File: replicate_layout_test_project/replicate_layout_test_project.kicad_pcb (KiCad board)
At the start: 2 copper layers, 69 parts, among them J1001 Pusa_6mm, J1002 Pusa_6mm, J201 Pusa_6mm, J202 Pusa_6mm, J601 Pusa_6mm, J602 Pusa_6mm, Q1101 CSD19531KCS, Q1102 CSD19531KCS, Q1301 CSD19531KCS, Q1302 CSD19531KCS, Q1401 CSD19531KCS, Q1402 CSD19531KCS, Q301 CSD19531KCS, Q302 CSD19531KCS, Q501 CSD19531KCS, Q502 CSD19531KCS, Q701 CSD19531KCS, Q702 CSD19531KCS, Q901 CSD19531KCS, Q902 CSD19531KCS, U101 TMS320F28027DA, U1101 IR2181, U1201 INA240A1D, U1301 IR2181, U1401 IR2181, U301 IR2181, U401 INA240A1D, U501 IR2181, U701 IR2181, U801 INA240A1D, U901 IR2181

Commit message: Towards flip replication
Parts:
- C702, Q701, Q702, R701, R702, U701: moved to B.Cu
- moved Q702 67.1 mm to (153.0, 65.9), turned to 135 degrees
- moved R702 63.6 mm to (148.9, 69.9), turned to 45 degrees
- moved C702 62.3 mm to (151.6, 78.0), turned to 135 degrees
- moved C701 60.9 mm to (145.3, 79.8), turned to -135 degrees
- moved U701 59.0 mm to (147.6, 81.1), turned to 45 degrees
- moved R701 57.2 mm to (157.0, 78.0), turned to 45 degrees
- moved D701 49.1 mm to (152.5, 82.5), turned to -135 degrees
- moved Q701 45.5 mm to (161.0, 74.0), turned to 125 degrees
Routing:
- net GND: track 103.8 -> 31.4 mm, vias 3 -> 1
- net /Full Bridge1/Leg+/VS: track 0.00 -> 30.9 mm
- net +15V: track 30.9 -> 10.3 mm, vias 3 -> 1
- net Net-(R702-Pad1): track 0.00 -> 13.7 mm
- net Net-(R701-Pad1): track 0.00 -> 7.89 mm
- net /Full Bridge1/Q_high: track 0.00 -> 7.46 mm
- net /Full Bridge1/Q_low: track 0.00 -> 6.82 mm
- net /Full Bridge1/Leg+/VB: track 0.00 -> 6.10 mm, vias 0 -> 1
- net Net-(Q702-Pad1): track 0.00 -> 4.22 mm
- net Net-(Q701-Pad1): track 0.00 -> 4.21 mm
- added copper zone on B.Cu, net /Full Bridge1/Leg+/VS

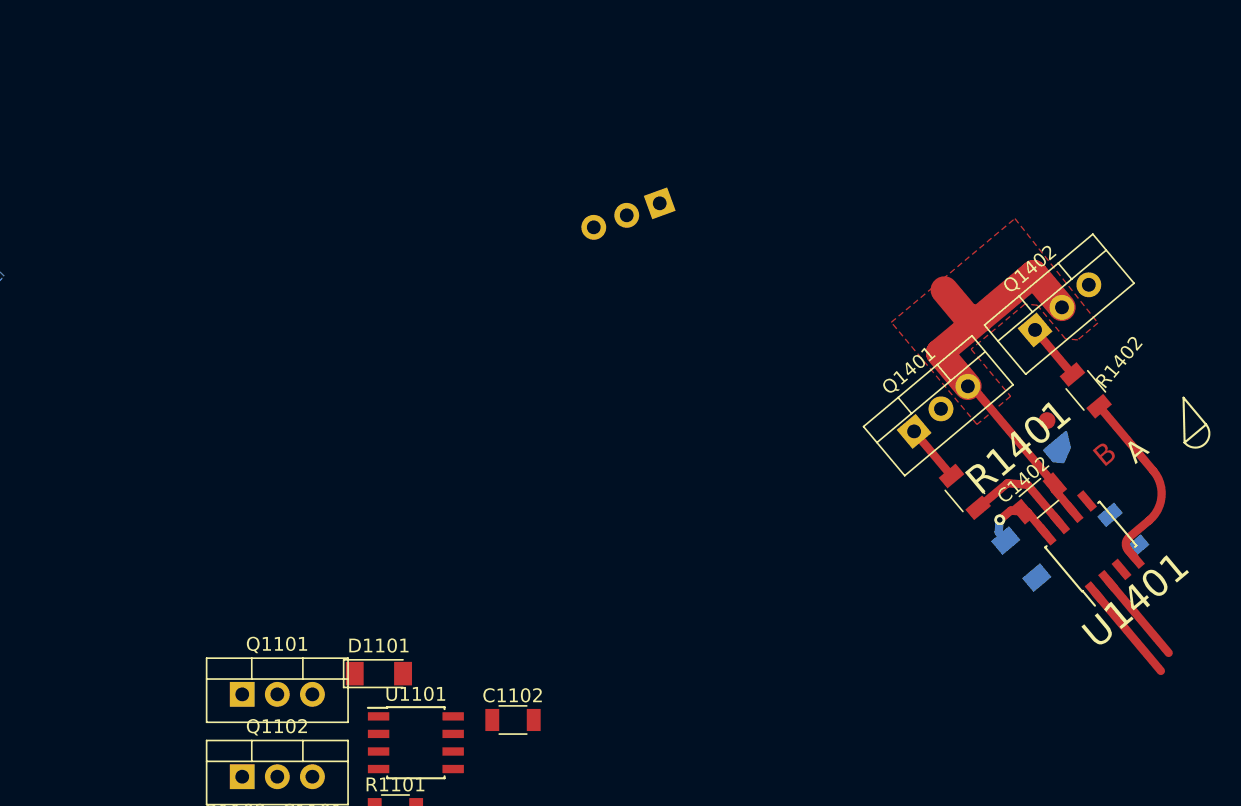
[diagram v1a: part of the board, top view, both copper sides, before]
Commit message: Solved fp_text replication
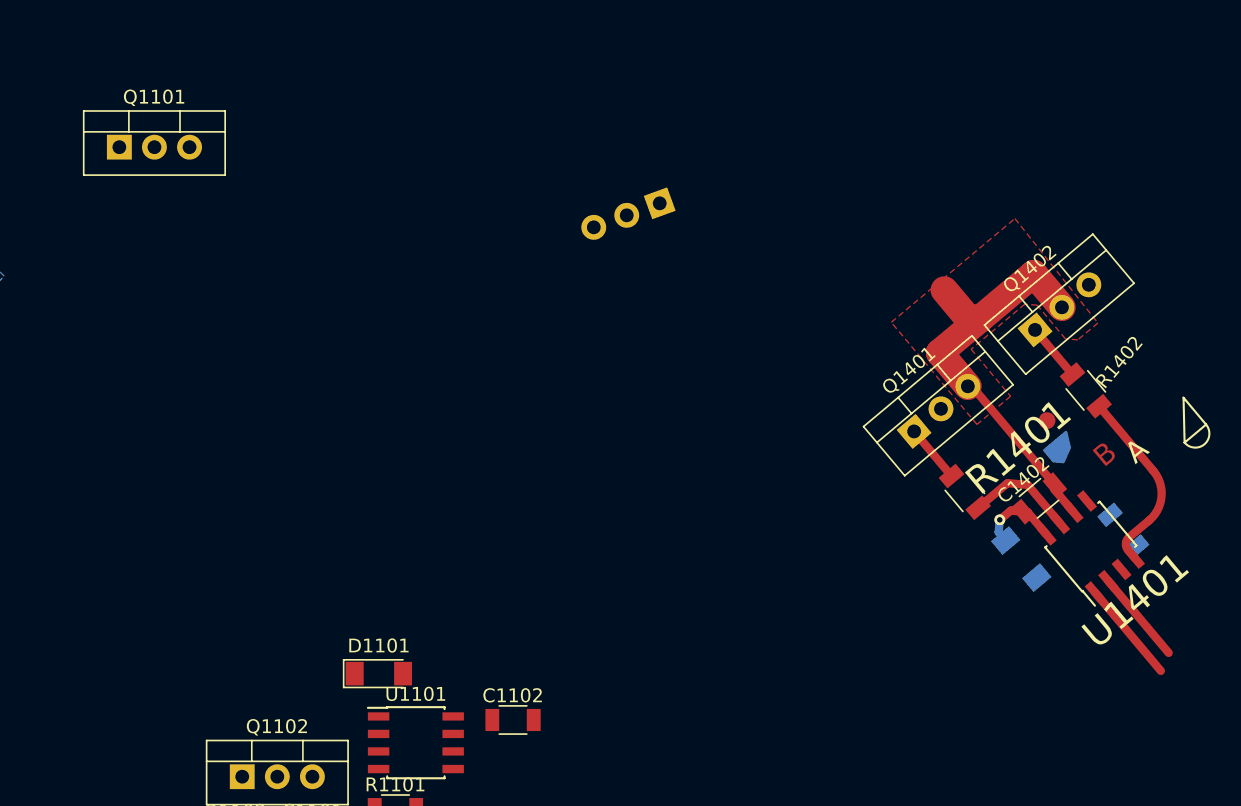
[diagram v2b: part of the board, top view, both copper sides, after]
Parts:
- moved Q1101 40.6 mm to (171.7, 56.9)
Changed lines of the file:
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@@
     (fp_line (start 1 -1.02) (end -1 -1.02) (layer "F.SilkS") (width 0.12))
     (fp_line (start -1 1.02) (end 1 1.02) (layer "F.SilkS") (width 0.12))
-    (fp_line (start 2.25 1.05) (end 2.25 -1.05) (layer "F.CrtYd") (width 0.05))
     (fp_line (start -2.25 -1.05) (end 2.25 -1.05) (layer "F.CrtYd") (width 0.05))
     (fp_line (start 2.25 1.05) (end -2.25 1.05) (layer "F.CrtYd") (width 0.05))
+    (fp_line (start 2.25 1.05) (end 2.25 -1.05) (layer "F.CrtYd") (width 0.05))
     (fp_line (start -2.25 -1.05) (end -2.25 1.05) (layer "F.CrtYd") (width 0.05))
     (fp_line (start 1.6 0.8) (end -1.6 0.8) (layer "F.Fab") (width 0.1))
@@
   )
   (footprint "Discretes:TO-220" (layer "F.Cu")
-    (at 180.6 96.505)
+    (at 171.704 56.896)
     (descr "TO-220-3, Vertical, RM 2.54mm")
     (tags "TO-220-3 Vertical RM 2.54mm")
@@
     ) (layer "B.Cu") (width 0.2) (fill solid))
   (gr_line (start 140.022201 71.620133) (end 141.818252 69.824082) (layer "B.SilkS") (width 0.15))
-  (gr_arc (start 141.459042 73.056974) (mid 140.022201 73.056975) (end 140.022201 71.620133) (layer "B.SilkS") (width 0.15))
+  (gr_arc (start 141.459042 73.056974) (mid 140.0222 73.056975) (end 140.022201 71.620133) (layer "B.SilkS") (width 0.15))
   (gr_line (start 141.818252 69.824082) (end 141.459042 73.056974) (layer "B.SilkS") (width 0.15))
   (gr_line (start 141.459042 73.056974) (end 140.022201 71.620133) (layer "B.SilkS") (width 0.15))
-  (gr_arc (start 250.372333 76.975492) (mid 250.247104 78.406865) (end 248.81573 78.281636) (layer "F.SilkS") (width 0.15))
+  (gr_arc (start 250.372333 76.975492) (mid 250.247103 78.406866) (end 248.81573 78.281636) (layer "F.SilkS") (width 0.15))
   (gr_line (start 250.372333 76.975492) (end 248.81573 78.281636) (layer "F.SilkS") (width 0.15))
   (gr_line (start 86.36 86.868) (end 86.36 89.408) (layer "F.SilkS") (width 0.15))
@@
   (arc (start 99.06 92.71) (mid 99.245987 92.260987) (end 99.695 92.075) (width 0.6) (layer "F.Cu") (net 40))
   (arc (start 101.6 92.075) (mid 103.396051 91.331051) (end 104.14 89.535) (width 0.6) (layer "F.Cu") (net 40))
+  (segment (start 153.975539 77.09809) (end 155.934225 79.056775) (width 0.6) (layer "B.Cu") (net 41))
   (segment (start 149.923817 79.679029) (end 152.504757 77.09809) (width 0.6) (layer "B.Cu") (net 41))
-  (segment (start 153.975539 77.09809) (end 155.934225 79.056775) (width 0.6) (layer "B.Cu") (net 41))
   (segment (start 152.504757 77.09809) (end 153.975539 77.09809) (width 0.6) (layer "B.Cu") (net 41))
   (segment (start 144.309389 81.701355) (end 144.871539 81.139205) (width 0.6) (layer "B.Cu") (net 42))

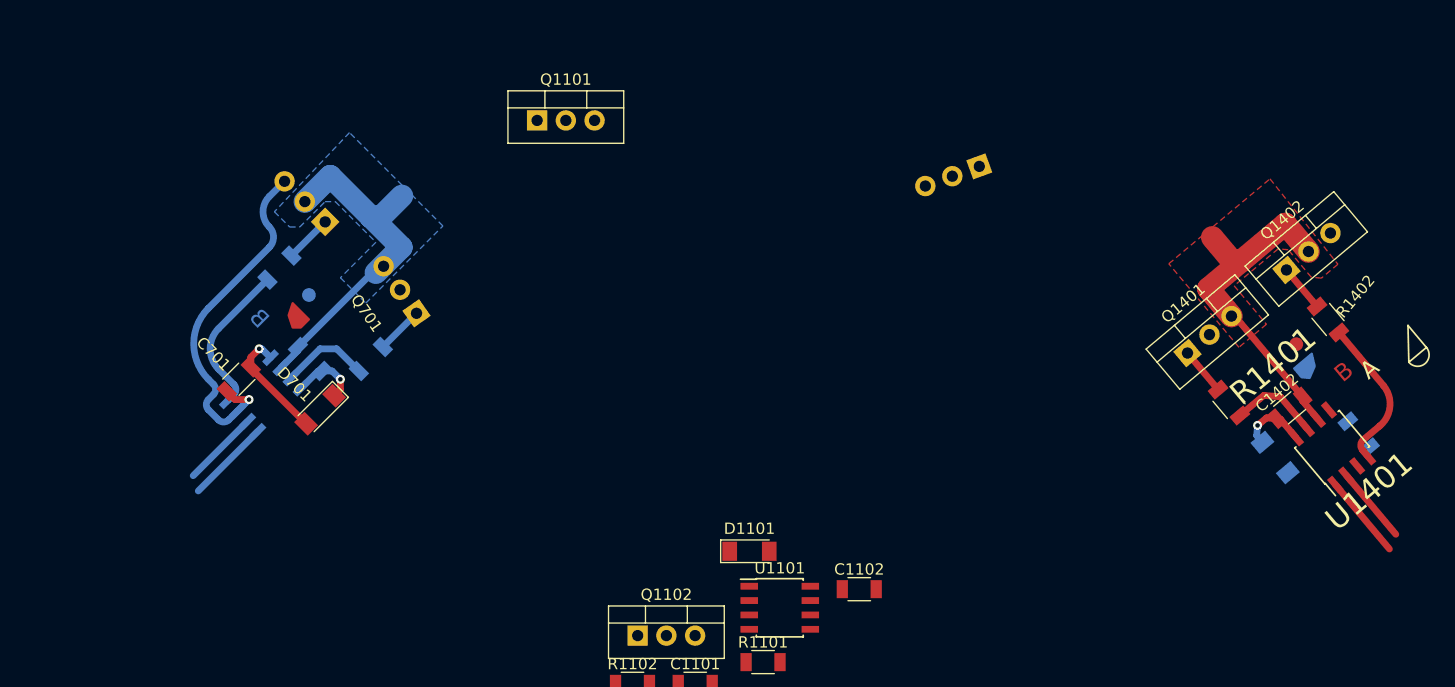
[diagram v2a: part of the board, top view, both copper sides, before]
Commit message: Added support for replicating grouped items only
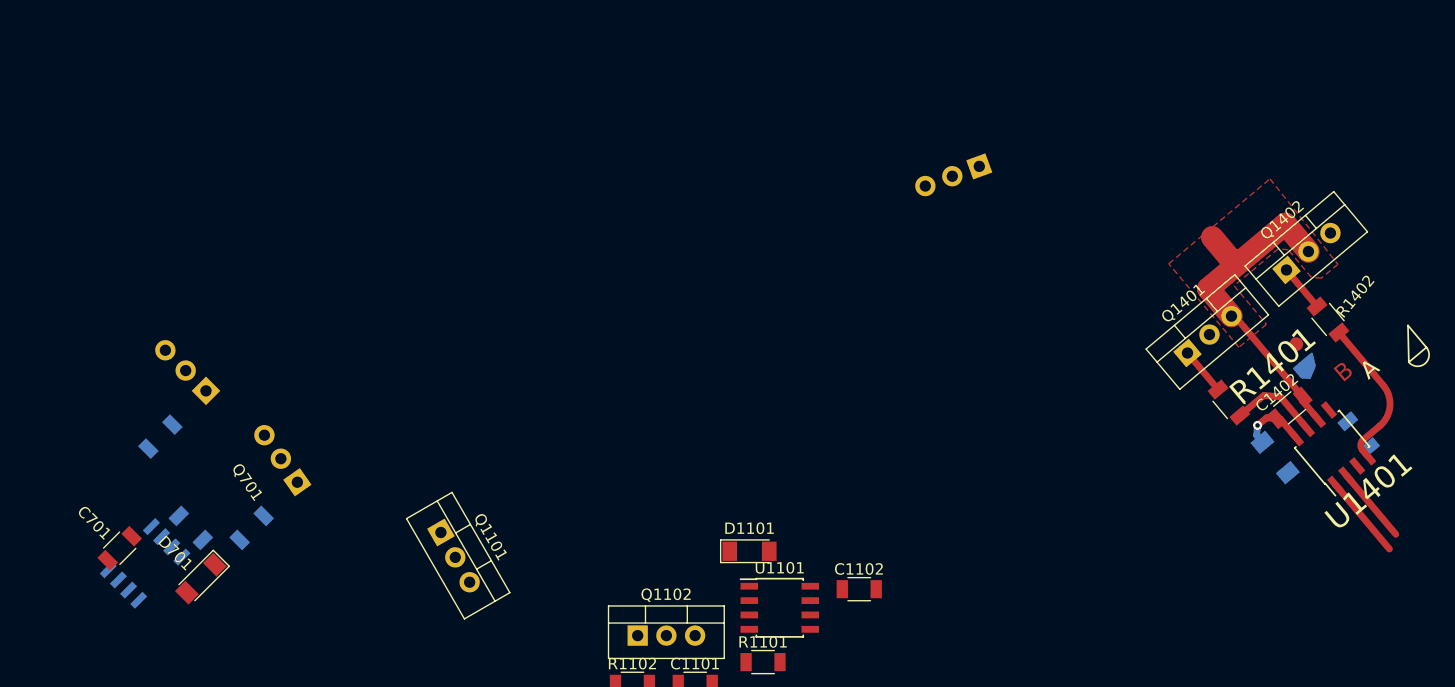
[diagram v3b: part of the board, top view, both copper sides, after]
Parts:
- moved Q1101 37.4 mm to (163.2, 93.3), turned to -60 degrees
- moved R701 18.3 mm to (146.5, 92.9)
- moved C701 18.3 mm to (134.8, 94.7)
- moved Q701 18.3 mm to (150.5, 88.9)
- moved R702 18.3 mm to (138.4, 84.9)
- moved C702 18.3 mm to (141.1, 92.9)
- moved D701 18.3 mm to (142.0, 97.4)
- moved Q702 18.3 mm to (142.4, 80.8)
- moved U701 18.3 mm to (137.0, 96.1)
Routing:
- net GND: track 31.4 -> 0.00 mm, vias 1 -> 0
- net /Full Bridge1/Leg+/VS: track 30.9 -> 0.00 mm
- net Net-(R702-Pad1): track 13.7 -> 0.00 mm
- net +15V: track 10.3 -> 0.00 mm, vias 1 -> 0
- net Net-(R701-Pad1): track 7.89 -> 0.00 mm
- net /Full Bridge1/Q_high: track 7.46 -> 0.00 mm
- net /Full Bridge1/Q_low: track 6.82 -> 0.00 mm
- net /Full Bridge1/Leg+/VB: track 6.10 -> 0.00 mm, vias 1 -> 0
- net Net-(Q702-Pad1): track 4.22 -> 0.00 mm
- net Net-(Q701-Pad1): track 4.21 -> 0.00 mm
- removed copper zone on B.Cu, net /Full Bridge1/Leg+/VS

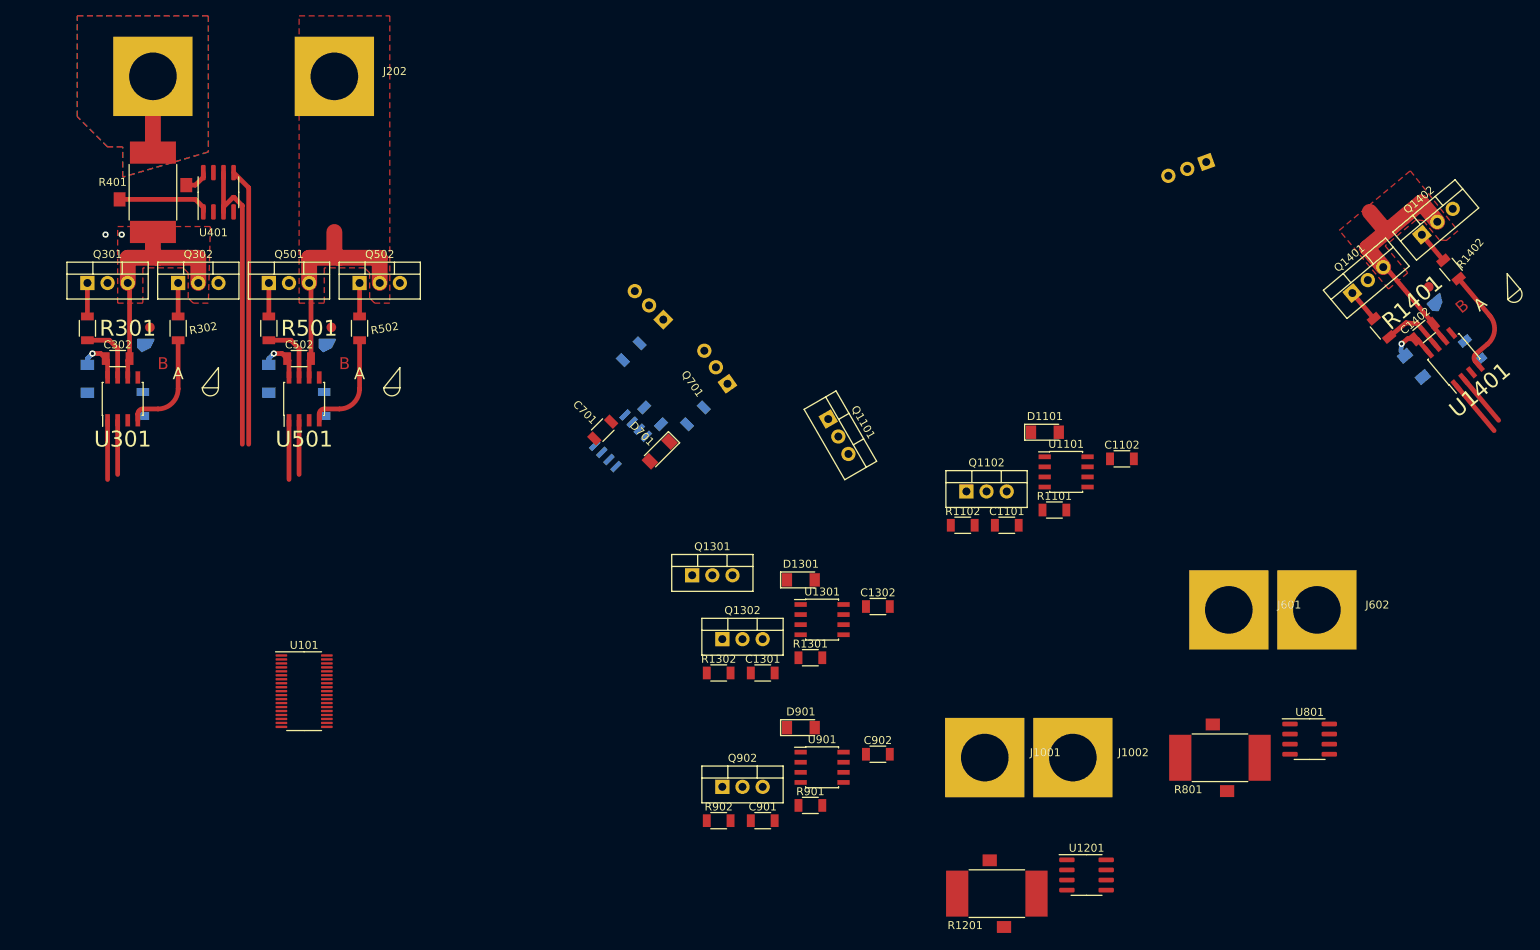
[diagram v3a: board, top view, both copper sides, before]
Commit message: Fix a bug when layout only footprints are present
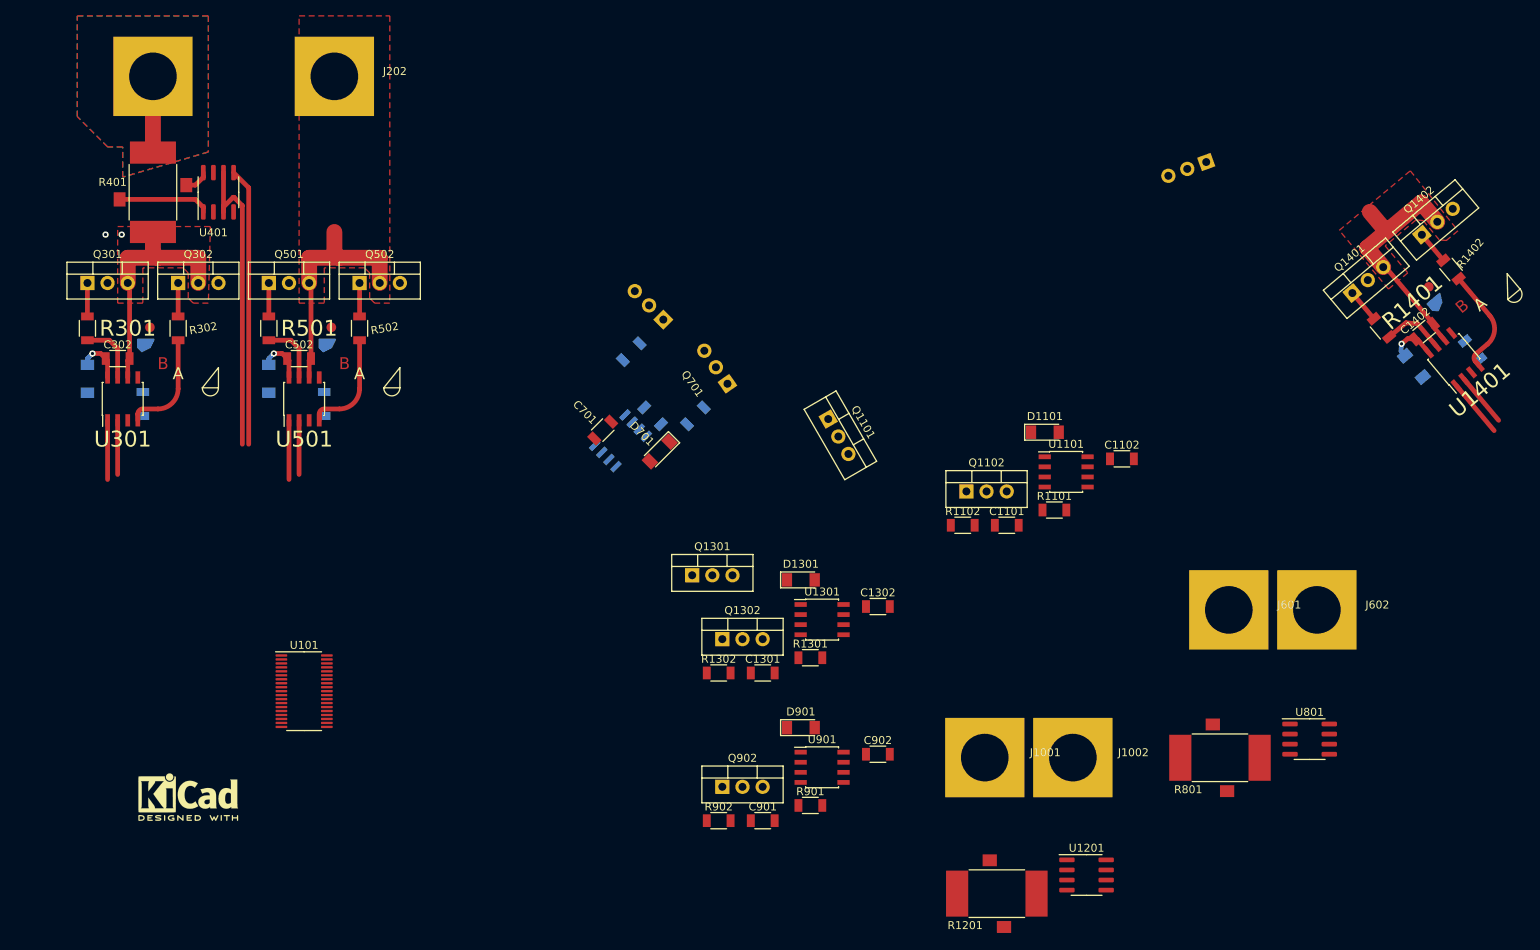
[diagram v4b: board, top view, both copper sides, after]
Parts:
- added REF**: KiCad-Logo2_5mm_SilkScreen, Symbol:KiCad-Logo2_5mm_SilkScreen, F.Cu at (82.5, 141.0)

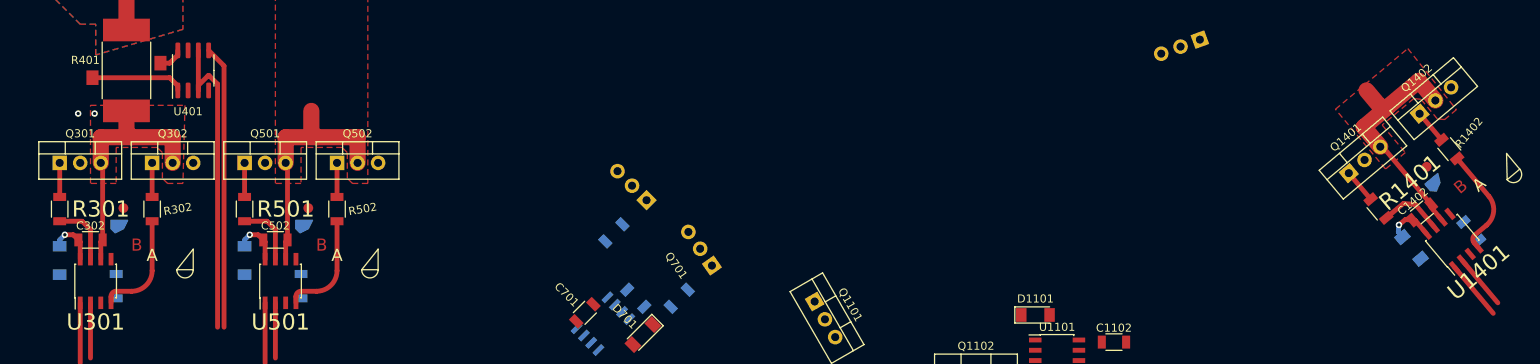
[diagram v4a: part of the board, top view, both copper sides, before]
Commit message: Minor logic bugfixes: - Keep destination sheet selection when changing settings - Replicate tracks which are completely local to source sheet   even if they are outside of bounding box - update test code and test project
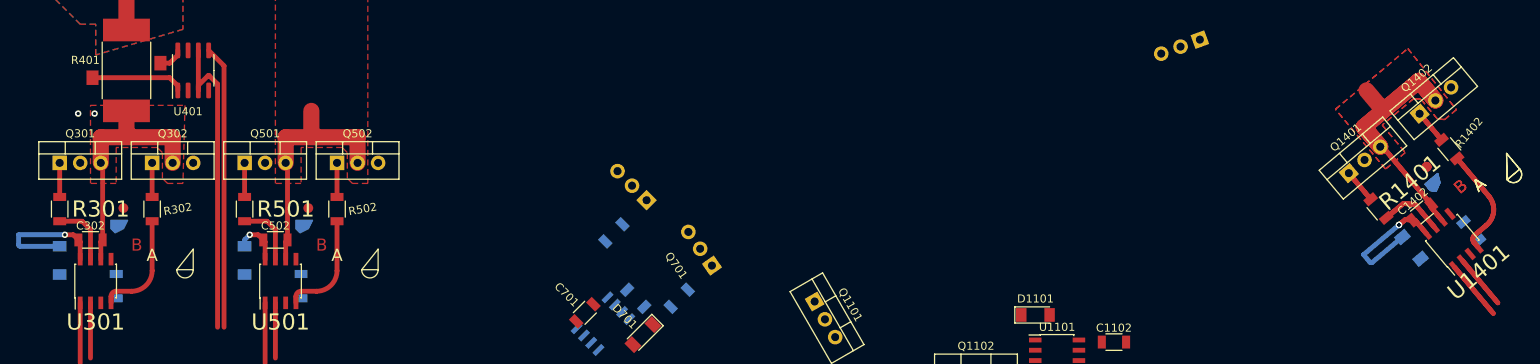
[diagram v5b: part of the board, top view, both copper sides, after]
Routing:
- net /Leg+1/VS: track 30.9 -> 59.1 mm
- net /Leg+1/VB: track 6.10 -> 21.0 mm, vias 1 -> 2
- net Net-(R1402-Pad1): track 13.7 -> 27.4 mm
- net /Full Bridge/Leg+/VB: track 6.10 -> 16.5 mm
- net Net-(R1401-Pad1): track 7.89 -> 15.8 mm
- net /Leg+1/Q_HIGH: track 7.46 -> 14.9 mm
- net /Leg+1/Q_LOW: track 6.83 -> 13.7 mm
- net Net-(Q1402-Pad1): track 4.21 -> 8.43 mm
- net Net-(Q1401-Pad1): track 4.21 -> 8.43 mm

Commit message: Dodal zaklenjen tekst
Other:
- board text added: "locked"
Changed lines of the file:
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@@
+    (effects (font (size 1.5 1.5) (thickness 0.3)))
+  )
+  (gr_text "locked" (at 82.55 91.44) (layer "B.Cu")
     (effects (font (size 1.5 1.5) (thickness 0.3)))
   )
